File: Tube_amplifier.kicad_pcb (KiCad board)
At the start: 2 copper layers, 150 x 50 mm, 34 parts, among them J2 Input, J3 Conn_01x04, J4 output, T1 Transformer_SP_1S, U1 6N2P, U2 6P14P

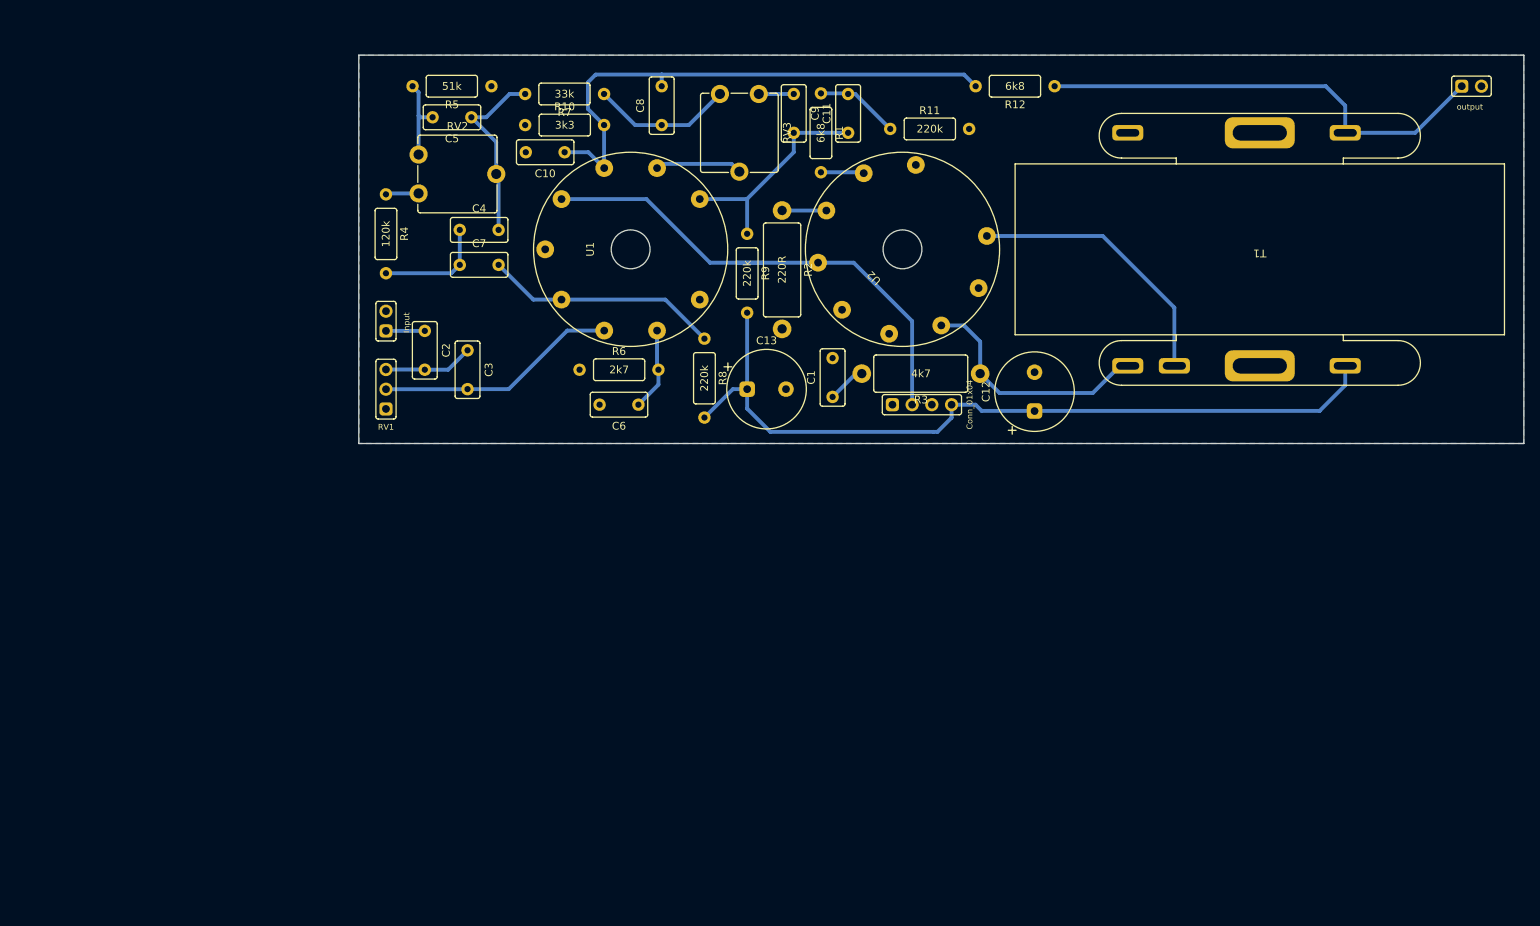
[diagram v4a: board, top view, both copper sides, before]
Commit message: Power supply added
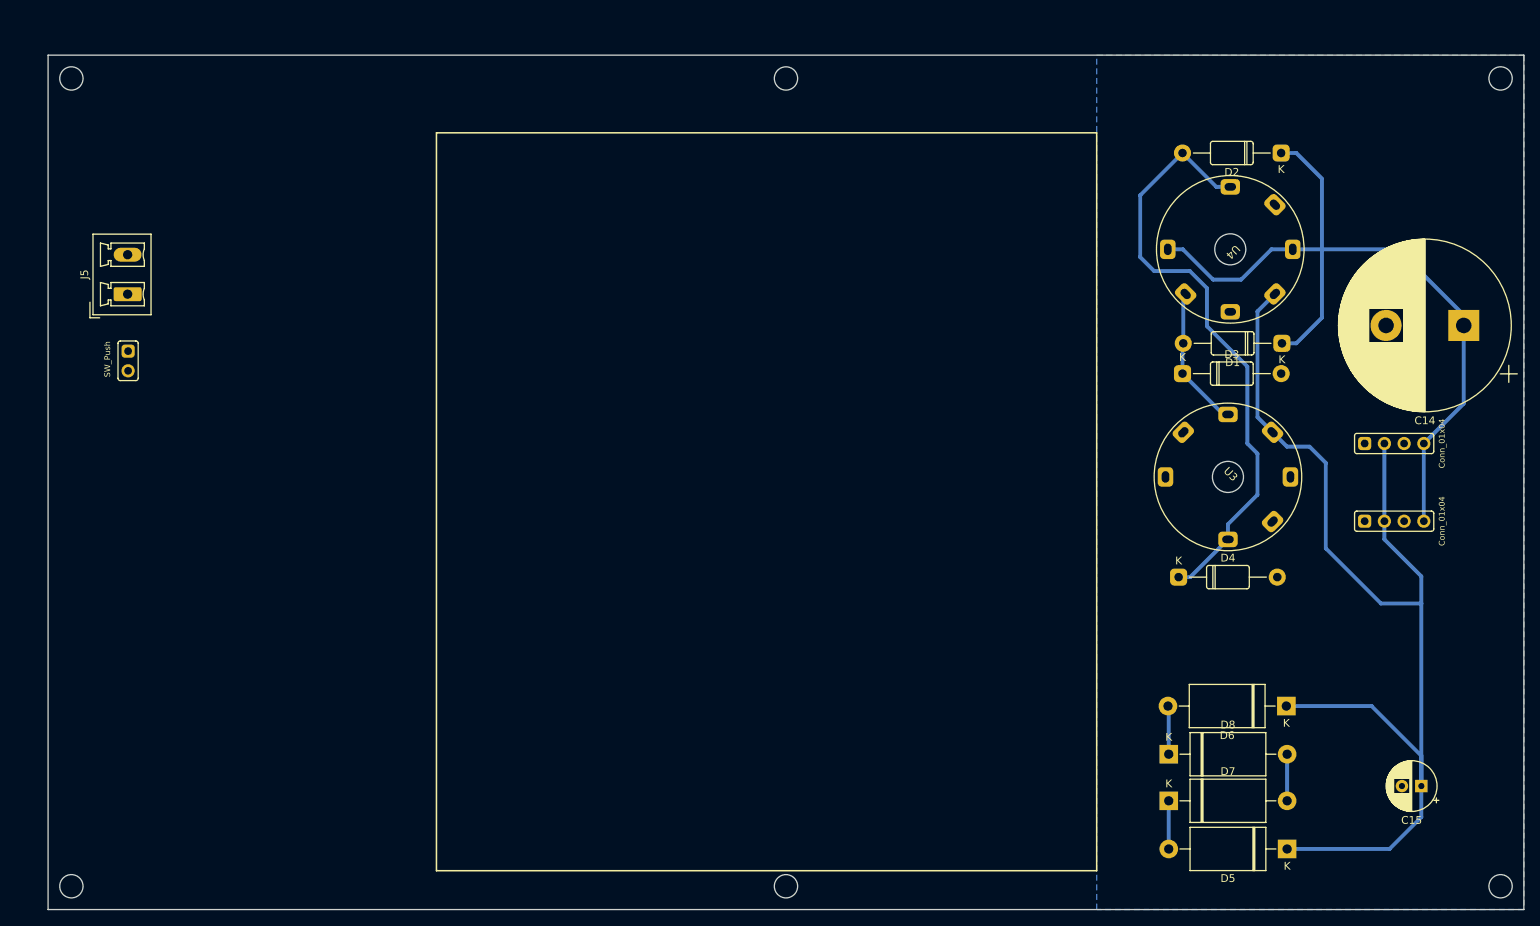
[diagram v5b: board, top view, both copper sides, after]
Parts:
- removed C1: 1500pF, spdf1626_lib:C_THT_K73-17_P5.00mm
- removed C10, C4, C8: 2200pF, spdf1626_lib:C_THT_K73-17_P5.00mm
- removed C11: 3300pF, spdf1626_lib:C_THT_K73-17_P5.00mm
- removed C12, C13: 10uF, spdf1626_lib:C_THT_D10.0mm_P5.00mm
- removed C2: 0,047uF, spdf1626_lib:C_THT_K73-17_P5.00mm
- removed C3: 27pF, spdf1626_lib:C_THT_K73-17_P5.00mm
- removed C5: 4700pF, spdf1626_lib:C_THT_K73-17_P5.00mm
- removed C6: 0,01uF, spdf1626_lib:C_THT_K73-17_P5.00mm
- removed C7: 0,033uF, spdf1626_lib:C_THT_K73-17_P5.00mm
- removed C9: 5,6pF, spdf1626_lib:C_THT_K73-17_P5.00mm
- removed J2: Input, spdf1626_lib:PinHeader_1x02_P2.54mm
- removed J4: output, spdf1626_lib:PinHeader_1x02_P2.54mm
- removed R1, R12: 6k8, spdf1626_lib:R_THT_025W
- removed R10: 3k3, spdf1626_lib:R_THT_025W
- removed R11, R8, R9: 220k, spdf1626_lib:R_THT_025W
- removed R2: 220R, spdf1626_lib:R_THT_1W
- removed R3: 4k7, spdf1626_lib:R_THT_1W
- removed R4: 120k, spdf1626_lib:R_THT_025W
- removed R5: 51k, spdf1626_lib:R_THT_025W
- removed R6: 2k7, spdf1626_lib:R_THT_025W
- removed R7: 33k, spdf1626_lib:R_THT_025W
- removed RV1: 470k, spdf1626_lib:PinHeader_1x03_P2.54mm
- removed RV2: 2,2M, spdf1626_lib:Potentiometer_THT_CA9V
- removed RV3: 1M, spdf1626_lib:Potentiometer_THT_CA9V
- removed T1: Transformer_SP_1S, spdf1626_lib:Output_transformer
- removed U1: 6N2P, spdf1626_lib:9-pin_tube_socket
- removed U2: 6P14P, spdf1626_lib:9-pin_tube_socket
- added C14: 100uF, Capacitor_THT:CP_Radial_D22.0mm_P10.00mm_SnapIn, F.Cu at (232.3, 54.8)
- added C15: 100uF_10V, Capacitor_THT:CP_Radial_D6.3mm_P2.50mm, F.Cu at (226.8, 114.1)
- added D1: 1n4007, spdf1626_lib:D_DO-41, F.Cu at (208.8, 57.1)
- added D2: 1n4007, spdf1626_lib:D_DO-41, F.Cu at (208.8, 32.6)
- added D3: 1n4007, spdf1626_lib:D_DO-41, F.Cu at (196.1, 61.0)
- added D4: 1n4007, spdf1626_lib:D_DO-41, F.Cu at (195.6, 87.2)
- added D5: 10A10, Diode_THT:D_DO-27_P15.24mm_Horizontal, F.Cu at (209.5, 122.2)
- added D6: 10A10, Diode_THT:D_DO-27_P15.24mm_Horizontal, F.Cu at (209.4, 103.8)
- added D7: 10A10, Diode_THT:D_DO-27_P15.24mm_Horizontal, F.Cu at (194.3, 116.0)
- added D8: 10A10, Diode_THT:D_DO-27_P15.24mm_Horizontal, F.Cu at (194.3, 110.0)
- added J5: 220V, Connector_Phoenix_MC_HighVoltage:PhoenixContact_MCV_1,5_2-G-5.08_1x02_P5.08mm_Vertical, F.Cu at (60.2, 50.8)
- added J7: Conn_01x04, spdf1626_lib:PinHeader_1x04_P2.54mm, F.Cu at (219.5, 80.0)
- added SW1: SW_Push, spdf1626_lib:PinHeader_1x02_P2.54mm, F.Cu at (60.3, 58.1)
- added U3: 6H2P, spdf1626_lib:7-pin_tube_socket, F.Cu at (201.9, 74.3)
- added U4: 6H2P, spdf1626_lib:7-pin_tube_socket, F.Cu at (202.2, 45.0)
- moved J3 61.0 mm to (219.5, 70.0)
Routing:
- net +6V: track 65.7 -> 147.3 mm
- net 240_1: track 0.00 -> 78.8 mm
- net Net-(C10-Pad1): track 70.3 -> 0.00 mm
- net Left_output: track 59.4 -> 0.00 mm
- net Net-(T1-Pad2): track 35.5 -> 0.00 mm
- net Net-(R3-Pad1): track 31.5 -> 0.00 mm
- net Net-(C3-Pad2): track 31.2 -> 0.00 mm
- net Net-(C7-Pad2): track 30.4 -> 0.00 mm
- net Net-(C11-Pad1): track 28.6 -> 0.00 mm
- net Net-(C4-Pad2): track 24.3 -> 0.00 mm
- net 240_2: track 0.00 -> 18.4 mm
- net Net-(C8-Pad1): track 18.2 -> 0.00 mm
- net Net-(C4-Pad1): track 14.4 -> 0.00 mm
- net Net-(C2-Pad2): track 11.5 -> 0.00 mm
- net Net-(RV3-Pad2): track 11.2 -> 0.00 mm
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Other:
- board size 150 x 50 mm -> 190 x 110 mm

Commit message: Indication board completed
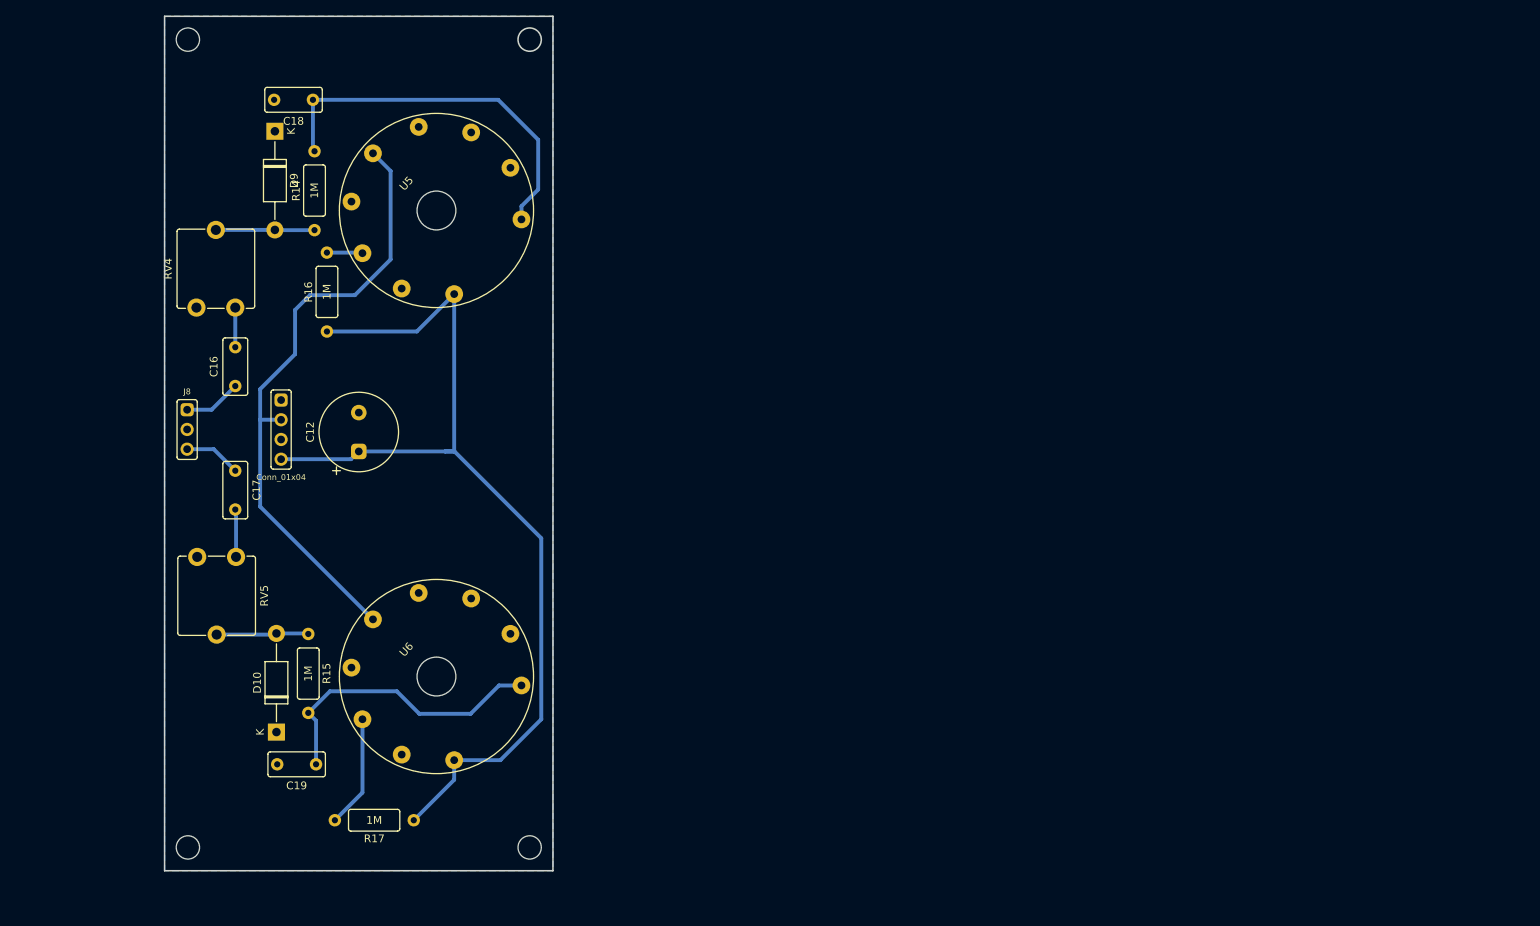
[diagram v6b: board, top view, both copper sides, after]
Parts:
- removed C14: 100uF, Capacitor_THT:CP_Radial_D22.0mm_P10.00mm_SnapIn
- removed C15: 100uF_10V, Capacitor_THT:CP_Radial_D6.3mm_P2.50mm
- removed D1, D2, D3, D4: 1n4007, spdf1626_lib:D_DO-41
- removed D5, D6, D7, D8: 10A10, Diode_THT:D_DO-27_P15.24mm_Horizontal
- removed J5: 220V, Connector_Phoenix_MC_HighVoltage:PhoenixContact_MCV_1,5_2-G-5.08_1x02_P5.08mm_Vertical
- removed J7: Conn_01x04, spdf1626_lib:PinHeader_1x04_P2.54mm
- removed SW1: SW_Push, spdf1626_lib:PinHeader_1x02_P2.54mm
- removed U3, U4: 6H2P, spdf1626_lib:7-pin_tube_socket
- added C12: 10uF, spdf1626_lib:C_THT_D10.0mm_P5.00mm, F.Cu at (90.0, 71.0)
- added C16: 6800pF, spdf1626_lib:C_THT_K73-17_P5.00mm, F.Cu at (74.1, 62.6)
- added C17: 6800pF, spdf1626_lib:C_THT_K73-17_P5.00mm, F.Cu at (74.1, 73.5)
- added C18: 6800pF, spdf1626_lib:C_THT_K73-17_P5.00mm, F.Cu at (84.1, 25.8)
- added C19: 6800pF, spdf1626_lib:C_THT_K73-17_P5.00mm, F.Cu at (84.5, 111.3)
- added D10: 1n4007, Diode_THT:D_DO-41_SOD81_P12.70mm_Horizontal, F.Cu at (79.4, 107.2)
- added D9: 1n4007, Diode_THT:D_DO-41_SOD81_P12.70mm_Horizontal, F.Cu at (79.2, 29.8)
- added J8: Indication, spdf1626_lib:PinHeader_1x03_P2.54mm, F.Cu at (67.9, 65.7)
- added R14: 1M, spdf1626_lib:R_THT_025W, F.Cu at (84.3, 42.5)
- added R15: 1M, spdf1626_lib:R_THT_025W, F.Cu at (83.5, 94.5)
- added R16: 1M, spdf1626_lib:R_THT_025W, F.Cu at (85.9, 55.6)
- added R17: 1M, spdf1626_lib:R_THT_025W, F.Cu at (97.1, 118.5)
- added RV4: 470k, spdf1626_lib:Potentiometer_THT_CA9V, F.Cu at (74.1, 52.5)
- added RV5: 470k, spdf1626_lib:Potentiometer_THT_CA9V, F.Cu at (69.2, 84.6)
- added U5: 6E1P, spdf1626_lib:9-pin_tube_socket, F.Cu at (100.0, 40.0)
- added U6: 6E1P, spdf1626_lib:9-pin_tube_socket, F.Cu at (100.0, 100.0)
- moved J3 139.6 mm to (80.0, 64.4), turned to 0 degrees
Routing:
- net 240_1: track 78.8 -> 0.00 mm
- net +6V: track 147.3 -> 80.0 mm
- net Net-(C18-Pad1): track 0.00 -> 49.0 mm
- net Net-(C19-Pad1): track 0.00 -> 38.3 mm
- net 240V: track 104.5 -> 124.9 mm
- net 240_2: track 18.4 -> 0.00 mm
- net Net-(R17-Pad2): track 0.00 -> 14.5 mm
- net Net-(D9-Pad2): track 0.00 -> 12.7 mm
- net Net-(D10-Pad2): track 0.00 -> 11.9 mm
- net Net-(C16-Pad1): track 0.00 -> 7.46 mm
- net Net-(C17-Pad1): track 0.00 -> 7.35 mm
- net Net-(D6-Pad2): track 6.24 -> 0.00 mm
- net Net-(D5-Pad2): track 6.20 -> 0.00 mm
- net Net-(C17-Pad2): track 0.00 -> 6.14 mm
- net GND: track 6.00 -> 0.00 mm
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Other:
- board size 190 x 110 mm -> 50 x 110 mm

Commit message: New schematic
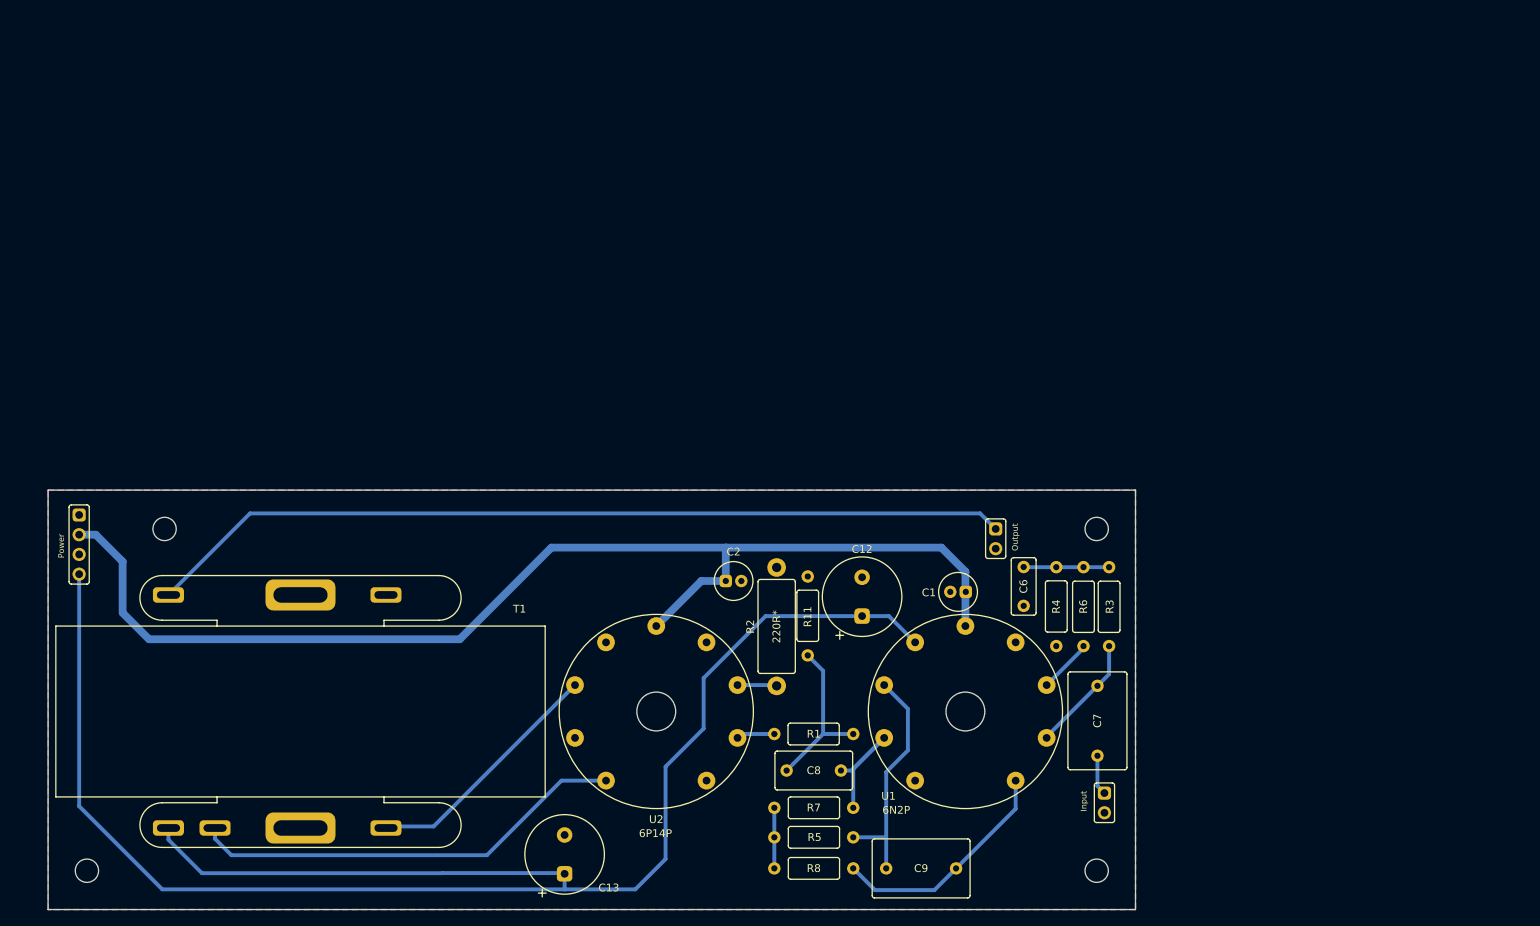
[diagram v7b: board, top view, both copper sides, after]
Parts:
- removed C16, C17, C18, C19: 6800pF, spdf1626_lib:C_THT_K73-17_P5.00mm
- removed D10, D9: 1n4007, Diode_THT:D_DO-41_SOD81_P12.70mm_Horizontal
- removed J8: Indication, spdf1626_lib:PinHeader_1x03_P2.54mm
- removed R14, R15, R16, R17: 1M, spdf1626_lib:R_THT_025W
- removed RV4, RV5: 470k, spdf1626_lib:Potentiometer_THT_CA9V
- removed U5, U6: 6E1P, spdf1626_lib:9-pin_tube_socket
- added C1: 10uF, spdf1626_lib:C_THT_D5.0mm_P2.00mm, F.Cu at (168.1, 89.1)
- added C13: 10uF, spdf1626_lib:C_THT_D10.0mm_P5.00mm, F.Cu at (116.5, 125.4)
- added C2: 10uF, spdf1626_lib:C_THT_D5.0mm_P2.00mm, F.Cu at (137.3, 87.7)
- added C6: 1n, spdf1626_lib:C_THT_K73-17_P5.00mm, F.Cu at (175.6, 85.9)
- added C7: 100n, spdf1626_lib:C_THT_K73-17_P9.00mm, F.Cu at (185.1, 105.7)
- added C8: 33n, spdf1626_lib:C_THT_K73-17_P7.00mm, F.Cu at (148.6, 112.1)
- added C9: 100n, spdf1626_lib:C_THT_K73-17_P9.00mm, F.Cu at (162.4, 124.7)
- added J2: Input, spdf1626_lib:PinHeader_1x02_P2.54mm, F.Cu at (186.0, 115.0)
- added J4: Output, spdf1626_lib:PinHeader_1x02_P2.54mm, F.Cu at (172.0, 81.0)
- added R1: 6k8, spdf1626_lib:R_THT_025W, F.Cu at (153.7, 107.4)
- added R11: 100k, spdf1626_lib:R_THT_025W, F.Cu at (147.8, 97.3)
- added R2: 220R*, spdf1626_lib:R_THT_1W, F.Cu at (143.8, 101.2)
- added R3: 300k, spdf1626_lib:R_THT_025W, F.Cu at (186.6, 85.9)
- added R4: 1k8, spdf1626_lib:R_THT_025W, F.Cu at (179.8, 96.1)
- added R5: 300k, spdf1626_lib:R_THT_025W, F.Cu at (143.5, 120.7)
- added R6: 200R, spdf1626_lib:R_THT_025W, F.Cu at (183.3, 85.9)
- added R7: 200R, spdf1626_lib:R_THT_025W, F.Cu at (143.5, 116.9)
- added R8: 1k8, spdf1626_lib:R_THT_025W, F.Cu at (143.5, 124.7)
- added T1: Transformer_SP_1S, spdf1626_lib:Output_transformer, F.Cu at (82.5, 104.5)
- added U1: 6N2P, spdf1626_lib:9-pin_tube_socket, F.Cu at (168.1, 104.5)
- added U2: 6P14P, spdf1626_lib:9-pin_tube_socket, F.Cu at (128.3, 104.5)
- J3: value Conn_01x04 -> Power
- moved C12 68.2 mm to (154.8, 92.2)
- moved J3 29.9 mm to (54.0, 79.2)
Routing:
- net Left_output: track 0.00 -> 111.7 mm
- net 240V: track 124.9 -> 225.0 mm
- net +6V: track 80.0 -> 152.4 mm
- net Net-(T1-Pad2): track 0.00 -> 56.6 mm
- net Net-(C18-Pad1): track 49.0 -> 0.00 mm
- net Net-(C19-Pad1): track 38.3 -> 0.00 mm
- net Net-(T1-Pad3): track 0.00 -> 32.0 mm
- net Net-(U1-Pad7): track 0.00 -> 30.3 mm
- net Net-(U1-Pad1): track 0.00 -> 30.0 mm
- net Net-(C8-Pad2): track 0.00 -> 21.5 mm
- net Net-(U1-Pad8): track 0.00 -> 18.5 mm
- net Net-(U1-Pad2): track 0.00 -> 15.2 mm
- net Net-(R17-Pad2): track 14.5 -> 0.00 mm
- net Net-(D9-Pad2): track 12.7 -> 0.00 mm
- net Net-(D10-Pad2): track 11.9 -> 0.00 mm
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- added copper zone on F.Cu, net GND
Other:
- board size 50 x 110 mm -> 140 x 54 mm
